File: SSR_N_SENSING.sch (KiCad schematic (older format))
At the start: 14 parts, among them J1 CONN_01X01, J2 CONN_01X01, Q1 BC850, U3 ACS722

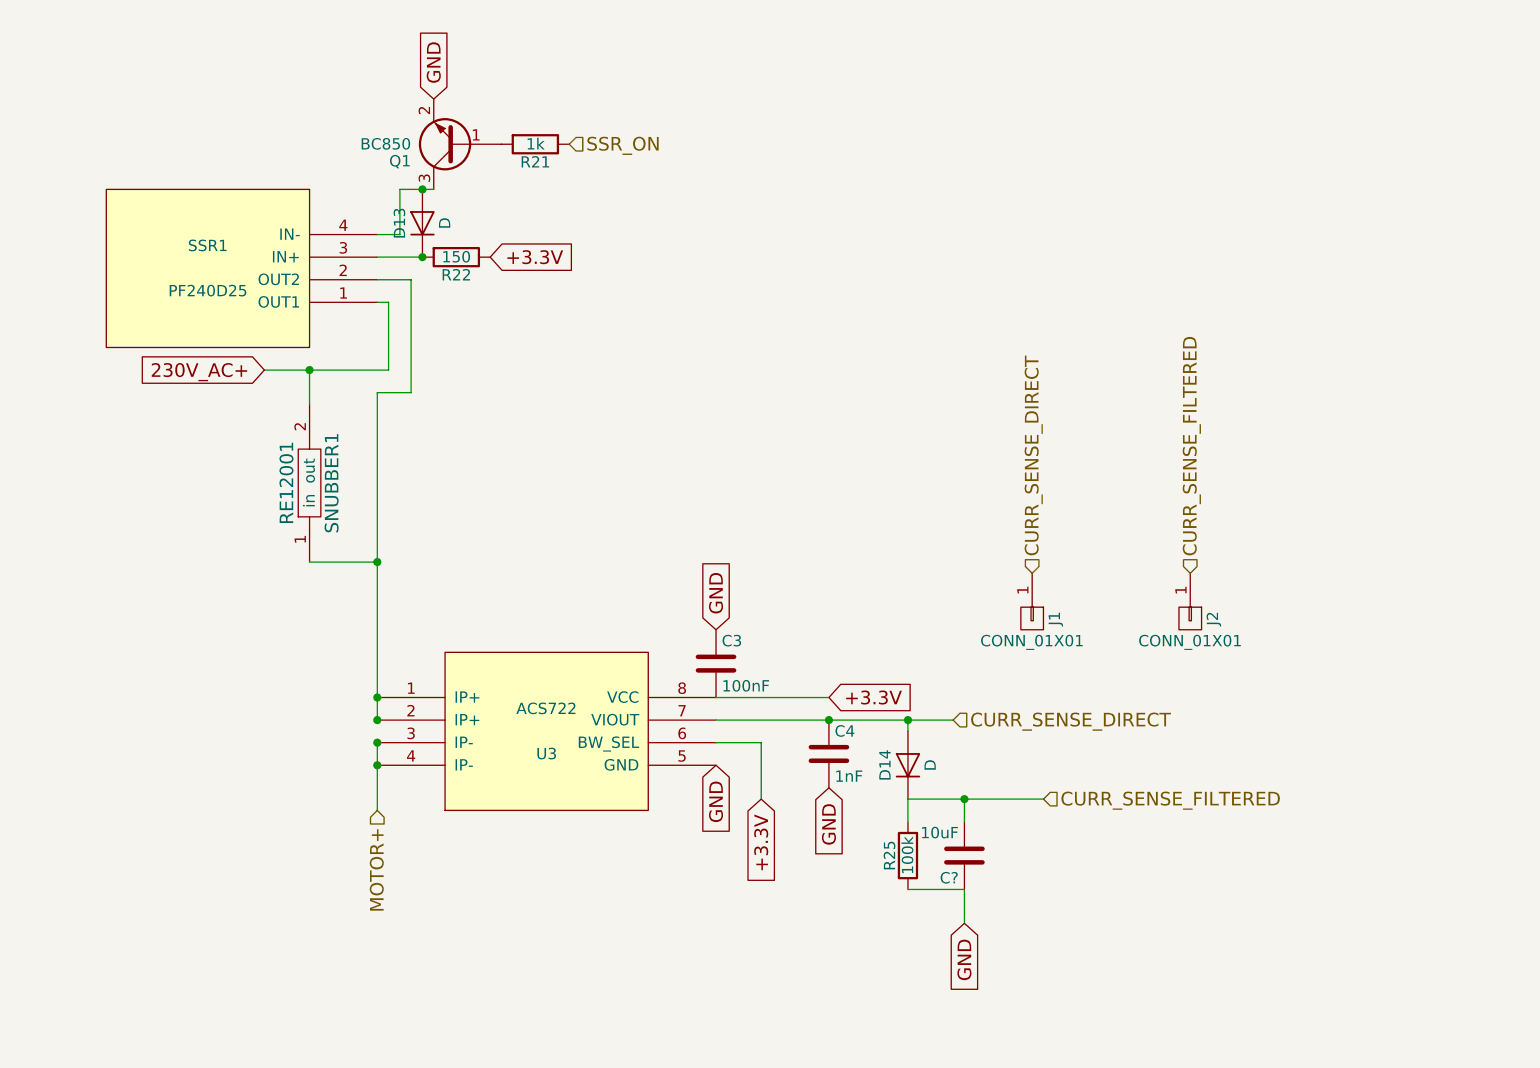
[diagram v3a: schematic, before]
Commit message: some issues fixed by the bugfixer; formal verification needed
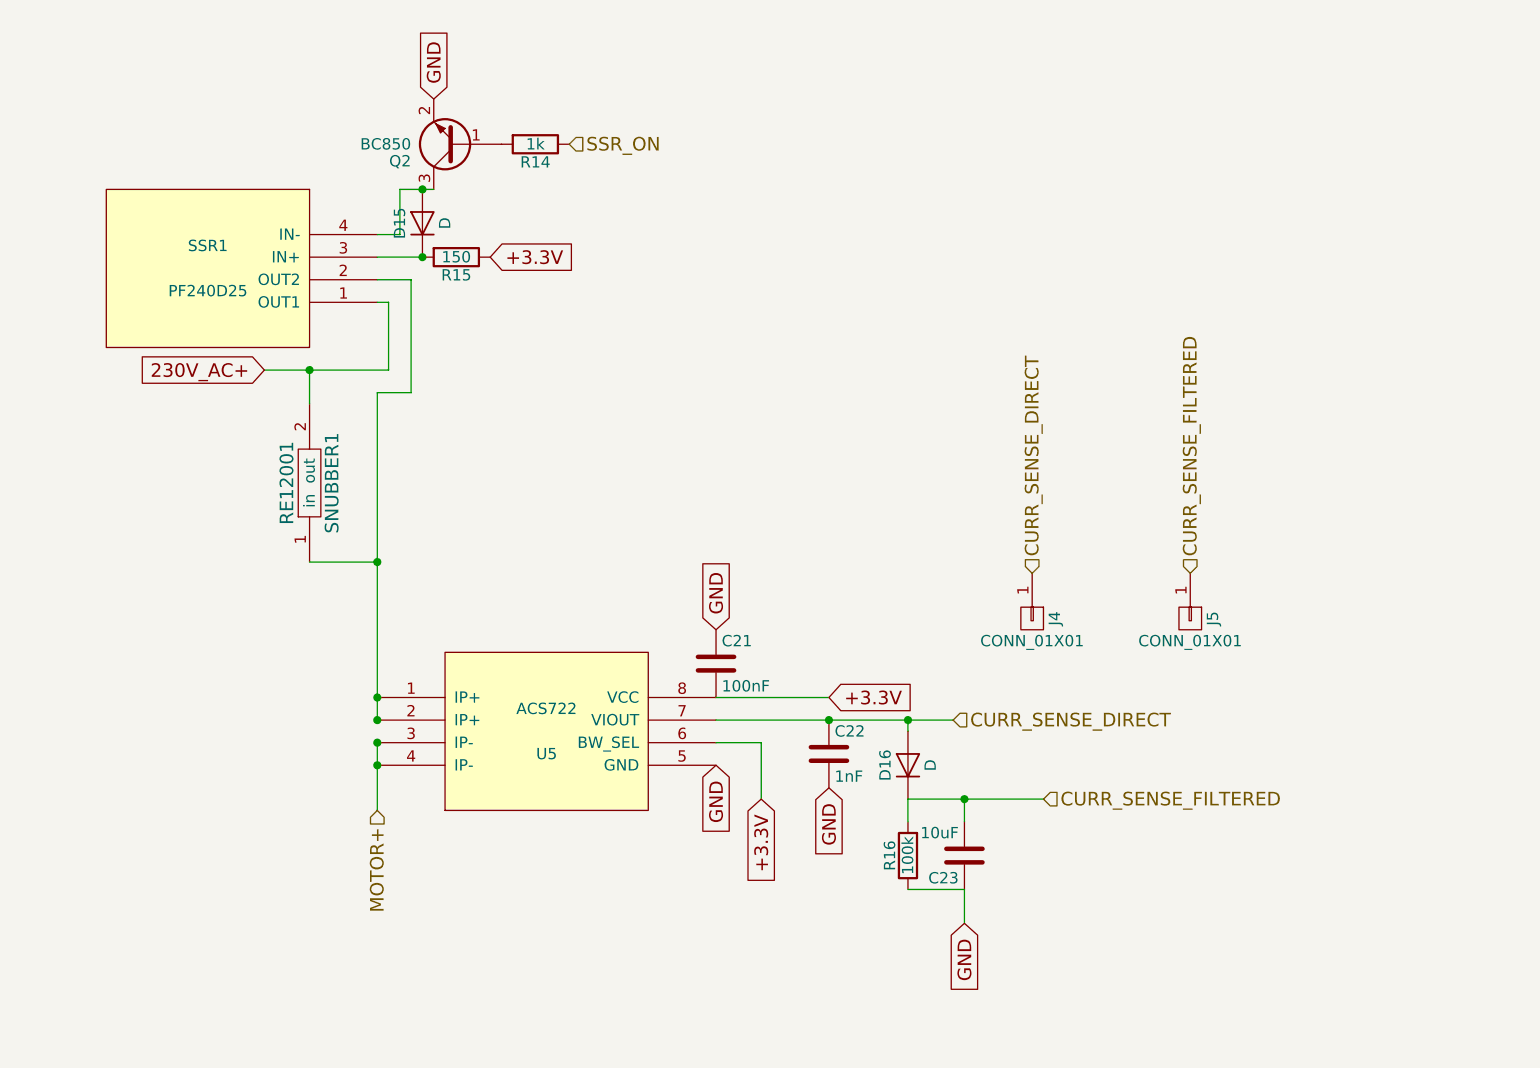
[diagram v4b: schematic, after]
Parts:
- gave numbers to parts that had none: 1
- renumbered C3 to C21, C4 to C22, D13 to D15, D14 to D16, J1 to J4, J2 to J5, Q1 to Q2, R21 to R14, R22 to R15, R25 to R16, U3 to U5
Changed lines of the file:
@@
 MOTOR+
 $Comp
-L D D13
+L D D15
 U 1 1 561BC3FC
 P 3650 2150
-F 0 "D13" H 3650 2250 50  0000 C CNN
+F 0 "D15" H 3650 2250 50  0000 C CNN
 F 1 "D" H 3650 2050 50  0000 C CNN
 F 2 "Diodes_SMD:D_SOD-123" H 3650 2150 60  0001 C CNN
@@
 $EndComp
 $Comp
-L R R22
+L R R15
 U 1 1 561BC4D2
 P 3800 2300
-F 0 "R22" V 3880 2300 50  0000 C CNN
+F 0 "R15" V 3880 2300 50  0000 C CNN
 F 1 "150" V 3800 2300 50  0000 C CNN
 F 2 "Resistors_SMD:R_0603_HandSoldering" V 3730 2300 30  0001 C CNN
@@
 $EndComp
 $Comp
-L R R21
+L R R14
 U 1 1 561BC5DF
 P 4150 1800
-F 0 "R21" V 4230 1800 50  0000 C CNN
+F 0 "R14" V 4230 1800 50  0000 C CNN
 F 1 "1k" V 4150 1800 50  0000 C CNN
 F 2 "Resistors_SMD:R_0603_HandSoldering" V 4080 1800 30  0001 C CNN
@@
 SSR_ON
 $Comp
-L BC850 Q1
+L BC850 Q2
 U 1 1 561BCA44
 P 3800 1800
-F 0 "Q1" H 4000 1875 50  0000 L CNN
+F 0 "Q2" H 4000 1875 50  0000 L CNN
 F 1 "BC850" H 4000 1800 50  0000 L CNN
 F 2 "Housings_SOT-23_SOT-143_TSOT-6:SOT-23" H 4000 1725 50  0001 L CIN
@@
 230V_AC+
 $Comp
-L ACS722 U3
+L ACS722 U5
 U 1 1 56251027
 P 4200 4400
-F 0 "U3" H 4200 4300 50  0000 C CNN
+F 0 "U5" H 4200 4300 50  0000 C CNN
 F 1 "ACS722" H 4200 4500 50  0000 C CNN
 F 2 "Housings_SOIC:SOIC-8_3.9x4.9mm_Pitch1.27mm" H 4200 4400 50  0001 C CNN
@@
 $EndComp
 $Comp
-L C C3
+L C C21
 U 1 1 562512DC
 P 4950 4100
-F 0 "C3" H 4975 4200 50  0000 L CNN
+F 0 "C21" H 4975 4200 50  0000 L CNN
 F 1 "100nF" H 4975 4000 50  0000 L CNN
 F 2 "Capacitors_SMD:C_0603_HandSoldering" H 4988 3950 30  0001 C CNN
@@
 $EndComp
 $Comp
-L C C4
+L C C22
 U 1 1 56251583
 P 5450 4500
-F 0 "C4" H 5475 4600 50  0000 L CNN
+F 0 "C22" H 5475 4600 50  0000 L CNN
 F 1 "1nF" H 5475 4400 50  0000 L CNN
 F 2 "Capacitors_SMD:C_0603_HandSoldering" H 5488 4350 30  0001 C CNN
@@
 $EndComp
 $Comp
-L D D14
+L D D16
 U 1 1 56251898
 P 5800 4550
-F 0 "D14" H 5800 4650 50  0000 C CNN
+F 0 "D16" H 5800 4650 50  0000 C CNN
 F 1 "D" H 5800 4450 50  0000 C CNN
 F 2 "Diodes_SMD:D_SOD-123" H 5800 4550 60  0001 C CNN
@@
 $EndComp
 $Comp
-L R R25
+L R R16
 U 1 1 5625189E
 P 5800 4950
-F 0 "R25" V 5880 4950 50  0000 C CNN
+F 0 "R16" V 5880 4950 50  0000 C CNN
 F 1 "100k" V 5800 4950 50  0000 C CNN
 F 2 "Resistors_SMD:R_0603_HandSoldering" V 5730 4950 30  0001 C CNN
@@
 Connection ~ 3450 3650
 $Comp
-L CONN_01X01 J1
+L CONN_01X01 J4
 U 1 1 59407490
 P 6350 3900
-F 0 "J1" H 6350 4000 50  0000 C CNN
+F 0 "J4" H 6350 4000 50  0000 C CNN
 F 1 "CONN_01X01" V 6450 3900 50  0000 C CNN
 F 2 "Connectors:PINTST" H 6350 3900 50  0001 C CNN
@@
 $EndComp
 $Comp
-L CONN_01X01 J2
+L CONN_01X01 J5
 U 1 1 59407553
 P 7050 3900
-F 0 "J2" H 7050 4000 50  0000 C CNN
+F 0 "J5" H 7050 4000 50  0000 C CNN
 F 1 "CONN_01X01" V 7150 3900 50  0000 C CNN
 F 2 "Connectors:PINTST" H 7050 3900 50  0001 C CNN
@@
 Connection ~ 5800 4350
 $Comp
-L C C?
+L C C23
 U 1 1 59A85C33
 P 6050 4950
-F 0 "C?" H 6075 5050 50  0000 L CNN
+F 0 "C23" H 6075 5050 50  0000 L CNN
 F 1 "10uF" H 6075 4850 50  0000 L CNN
 F 2 "Capacitors_SMD:C_0603_HandSoldering" H 6088 4800 30  0001 C CNN

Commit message: part numbers generated;
pcb generation started
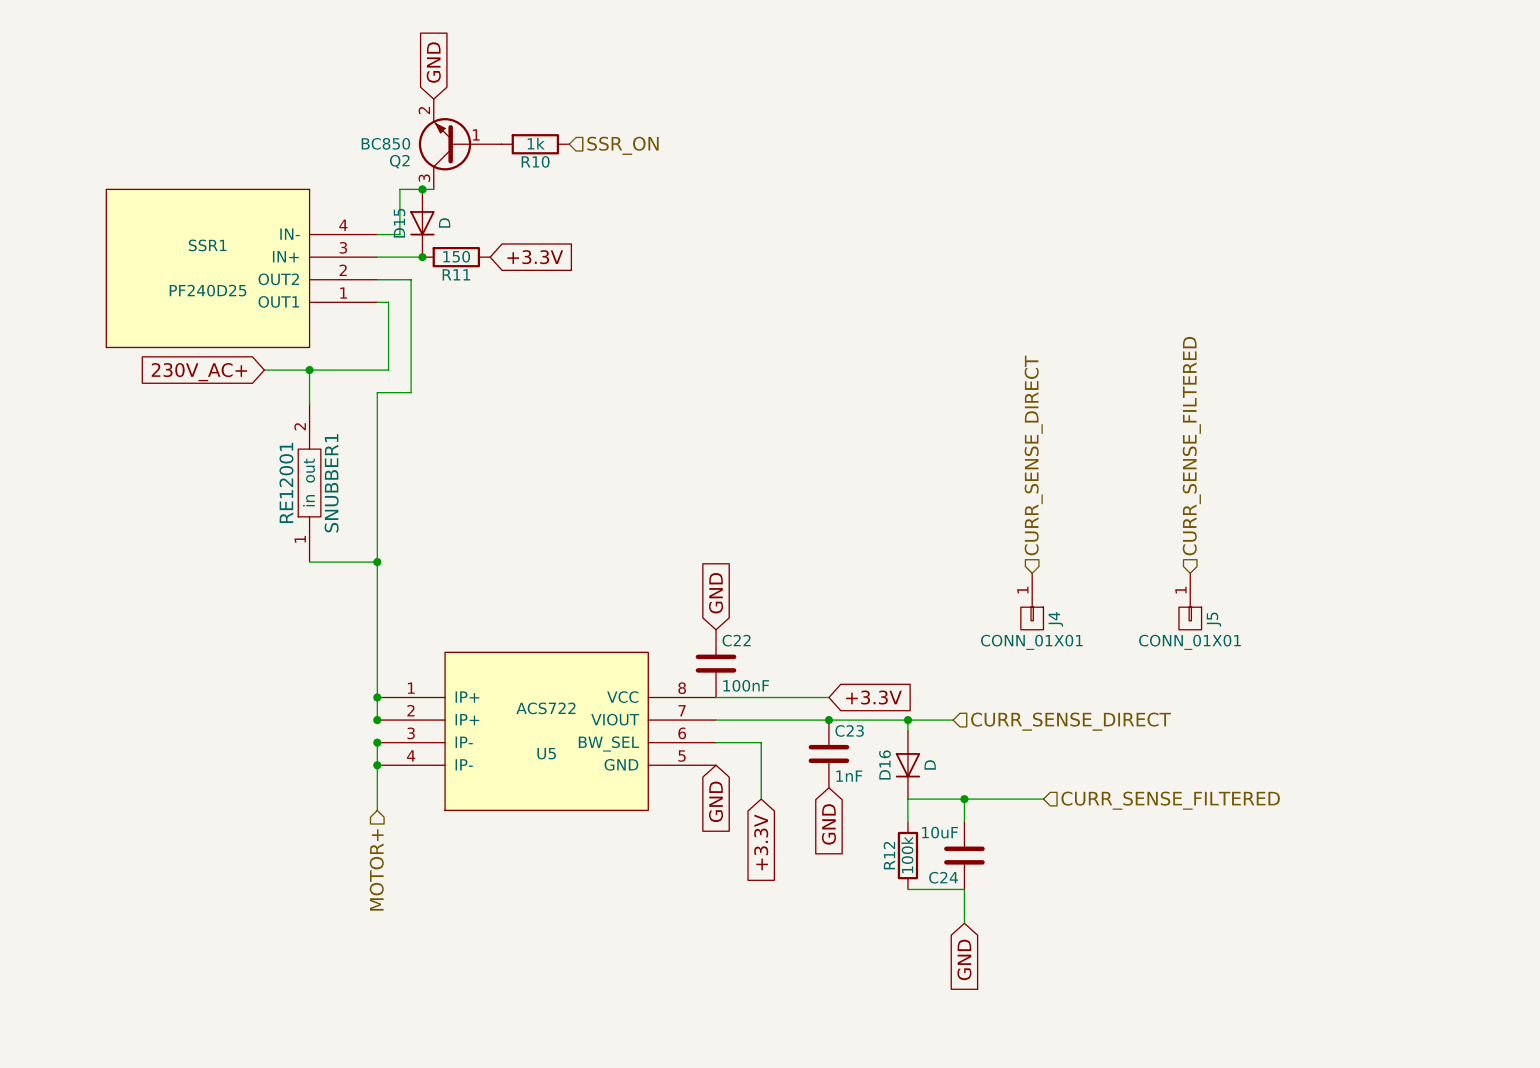
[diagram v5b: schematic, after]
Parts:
- renumbered C21 to C22, C22 to C23, C23 to C24, R14 to R10, R15 to R11, R16 to R12
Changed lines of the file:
@@
 $EndComp
 $Comp
-L R R15
+L R R11
 U 1 1 561BC4D2
 P 3800 2300
-F 0 "R15" V 3880 2300 50  0000 C CNN
+F 0 "R11" V 3880 2300 50  0000 C CNN
 F 1 "150" V 3800 2300 50  0000 C CNN
 F 2 "Resistors_SMD:R_0603_HandSoldering" V 3730 2300 30  0001 C CNN
@@
 $EndComp
 $Comp
-L R R14
+L R R10
 U 1 1 561BC5DF
 P 4150 1800
-F 0 "R14" V 4230 1800 50  0000 C CNN
+F 0 "R10" V 4230 1800 50  0000 C CNN
 F 1 "1k" V 4150 1800 50  0000 C CNN
 F 2 "Resistors_SMD:R_0603_HandSoldering" V 4080 1800 30  0001 C CNN
@@
 $EndComp
 $Comp
-L C C21
+L C C22
 U 1 1 562512DC
 P 4950 4100
-F 0 "C21" H 4975 4200 50  0000 L CNN
+F 0 "C22" H 4975 4200 50  0000 L CNN
 F 1 "100nF" H 4975 4000 50  0000 L CNN
 F 2 "Capacitors_SMD:C_0603_HandSoldering" H 4988 3950 30  0001 C CNN
@@
 $EndComp
 $Comp
-L C C22
+L C C23
 U 1 1 56251583
 P 5450 4500
-F 0 "C22" H 5475 4600 50  0000 L CNN
+F 0 "C23" H 5475 4600 50  0000 L CNN
 F 1 "1nF" H 5475 4400 50  0000 L CNN
 F 2 "Capacitors_SMD:C_0603_HandSoldering" H 5488 4350 30  0001 C CNN
@@
 $EndComp
 $Comp
-L R R16
+L R R12
 U 1 1 5625189E
 P 5800 4950
-F 0 "R16" V 5880 4950 50  0000 C CNN
+F 0 "R12" V 5880 4950 50  0000 C CNN
 F 1 "100k" V 5800 4950 50  0000 C CNN
 F 2 "Resistors_SMD:R_0603_HandSoldering" V 5730 4950 30  0001 C CNN
@@
 Connection ~ 5800 4350
 $Comp
-L C C23
+L C C24
 U 1 1 59A85C33
 P 6050 4950
-F 0 "C23" H 6075 5050 50  0000 L CNN
+F 0 "C24" H 6075 5050 50  0000 L CNN
 F 1 "10uF" H 6075 4850 50  0000 L CNN
 F 2 "Capacitors_SMD:C_0603_HandSoldering" H 6088 4800 30  0001 C CNN

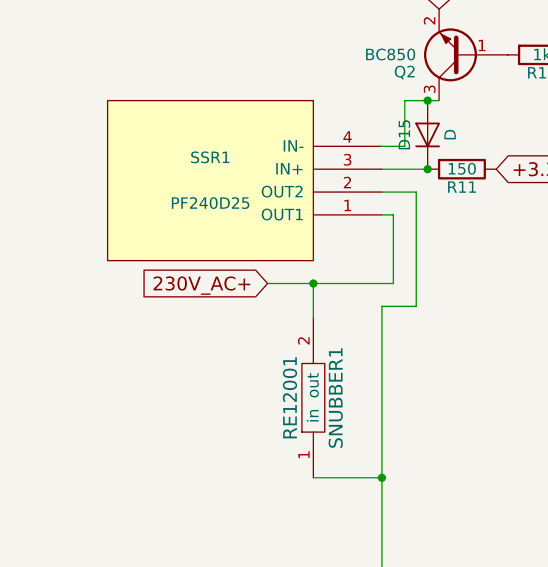
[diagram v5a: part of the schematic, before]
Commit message: fuse protected ssr circle
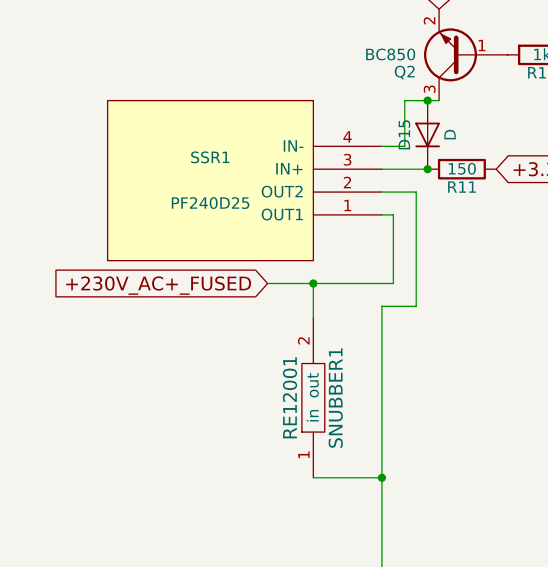
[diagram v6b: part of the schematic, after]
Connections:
- net 230V_AC+ renamed +230V_AC+_FUSED
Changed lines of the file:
@@
 	-1   0    0    1
 $EndComp
-Text GLabel 2950 2800 0    60   Input ~ 0
-230V_AC+
 $Comp
 L ACS722 U5
@@
 Wire Wire Line
 	5800 5100 6050 5100
+Text GLabel 2950 2800 0    60   Input ~ 0
++230V_AC+_FUSED
 $EndSCHEMATC

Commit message: all the components placed I nead to beautify
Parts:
- J4: value CONN_01X01 -> CURR_DIRECT
- J5: value CONN_01X01 -> CURR_FILT
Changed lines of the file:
@@
 P 6350 3900
 F 0 "J4" H 6350 4000 50  0000 C CNN
-F 1 "CONN_01X01" V 6450 3900 50  0000 C CNN
+F 1 "CURR_DIRECT" V 6450 3900 50  0000 C CNN
 F 2 "Connectors:PINTST" H 6350 3900 50  0001 C CNN
 F 3 "" H 6350 3900 50  0001 C CNN
@@
 P 7050 3900
 F 0 "J5" H 7050 4000 50  0000 C CNN
-F 1 "CONN_01X01" V 7150 3900 50  0000 C CNN
+F 1 "CURR_FILT" V 7150 3900 50  0000 C CNN
 F 2 "Connectors:PINTST" H 7050 3900 50  0001 C CNN
 F 3 "" H 7050 3900 50  0001 C CNN
